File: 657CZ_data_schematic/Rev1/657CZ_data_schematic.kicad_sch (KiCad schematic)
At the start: 0 parts

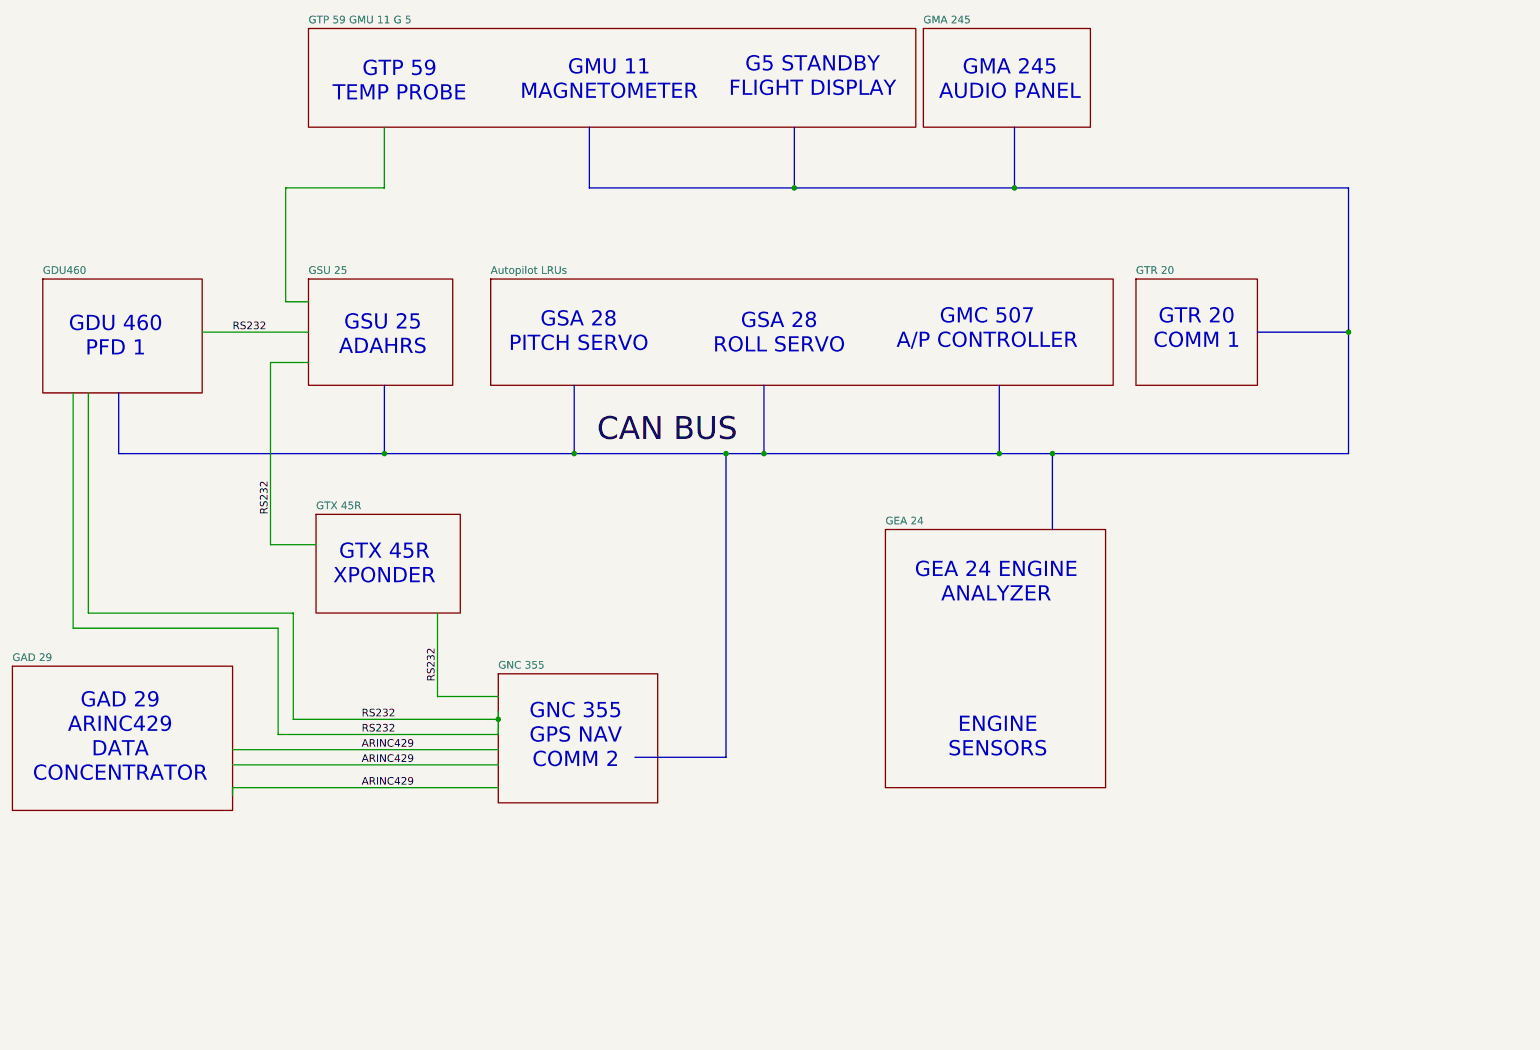
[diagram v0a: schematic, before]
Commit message: added data connections after AvClassics wiring. completed LRUs GMU, GDU, GSU, GAD, GNC, GTX, GTR  Not completed GMA, GEA and autopilot LRUs
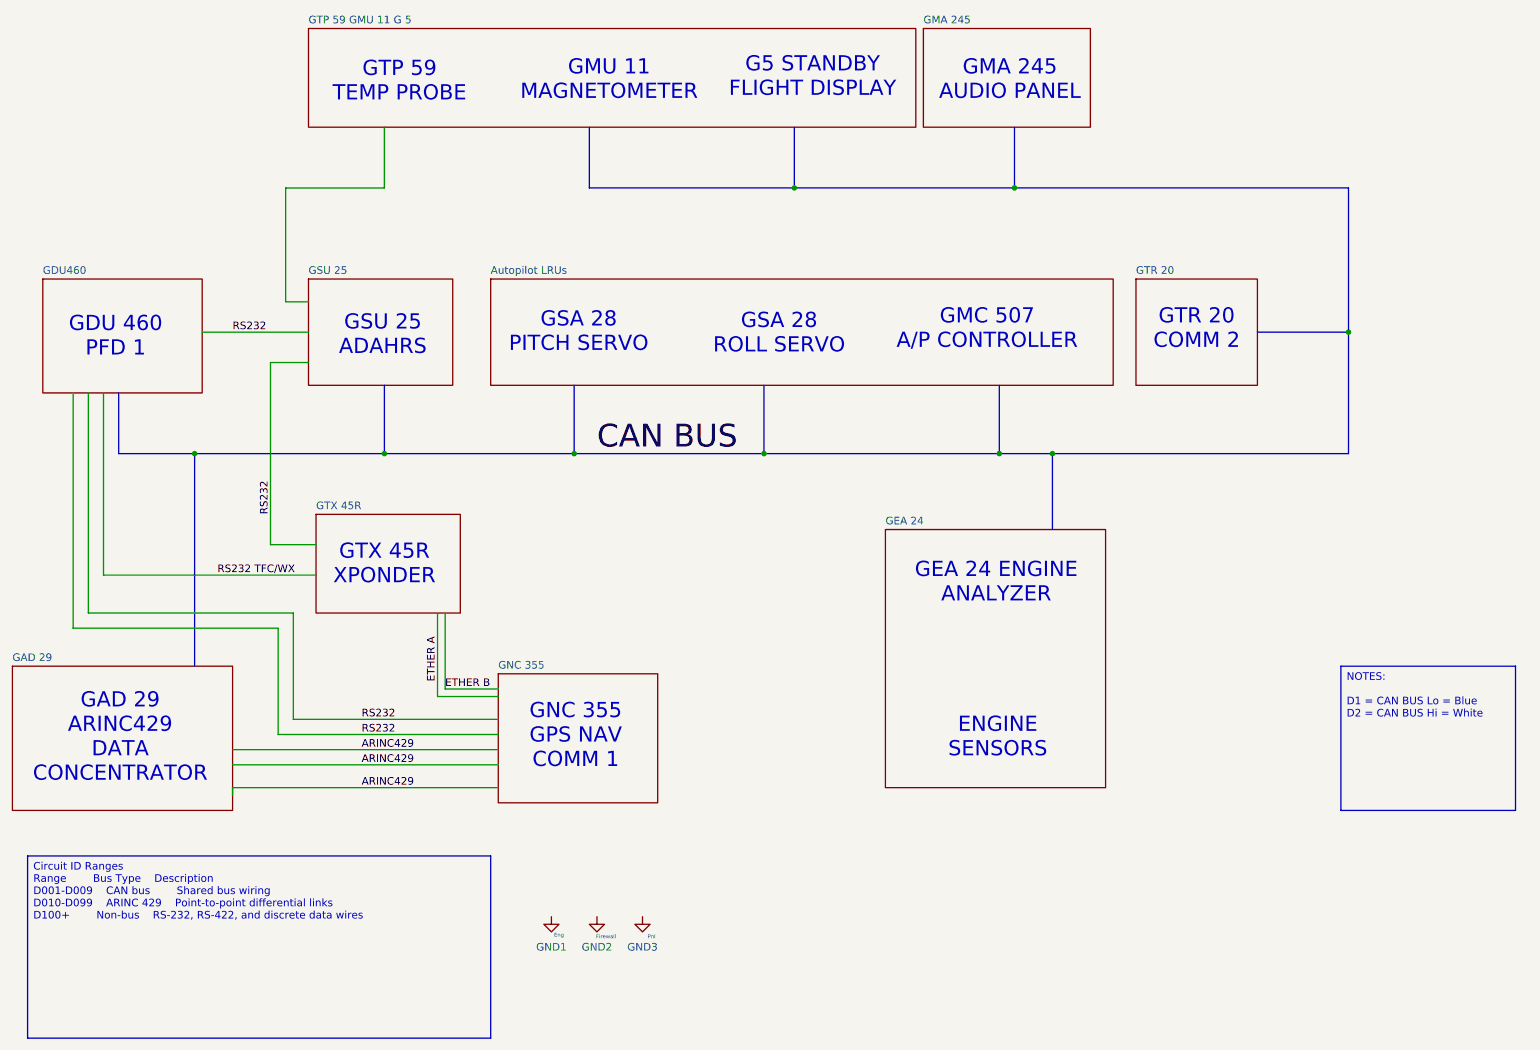
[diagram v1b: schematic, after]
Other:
- note added: "GNC 355 GPS NAV COMM 1"
- note added: "GTR 20 COMM 2"
- note removed: "GNC 355 GPS NAV COMM 2"
- note removed: "GTR 20 COMM 1"
